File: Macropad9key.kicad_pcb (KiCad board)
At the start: 4 copper layers, 57.9 x 65.7 mm, 83 parts, among them J1 3220-10-0100-00, J2 4POS_2MM, J3 USB4085-GF-A, SW1 CherryMX_WithPCBPins, SW2 CherryMX_WithPCBPins, SW3 CherryMX_WithPCBPins, SW4 CherryMX_WithPCBPins, SW5 CherryMX_WithPCBPins, SW6 CherryMX_WithPCBPins, SW7 CherryMX_WithPCBPins, SW8 CherryMX_WithPCBPins, SW9 CherryMX_WithPCBPins, U1 ATSAMD11D14A-MUT, U2 MCP1700T-3302E-TT, U3 PCA9632DP2

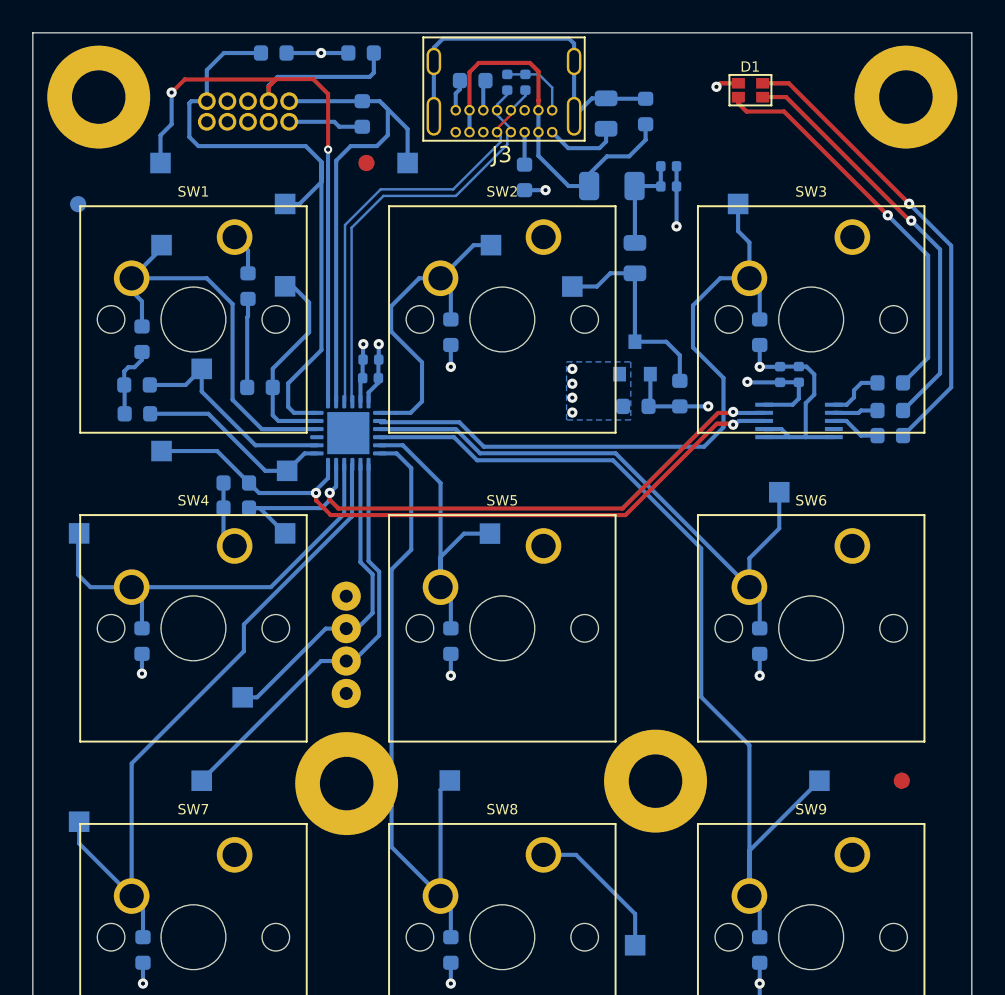
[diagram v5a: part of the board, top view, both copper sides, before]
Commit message: Fix mounting screw hole under ICD header
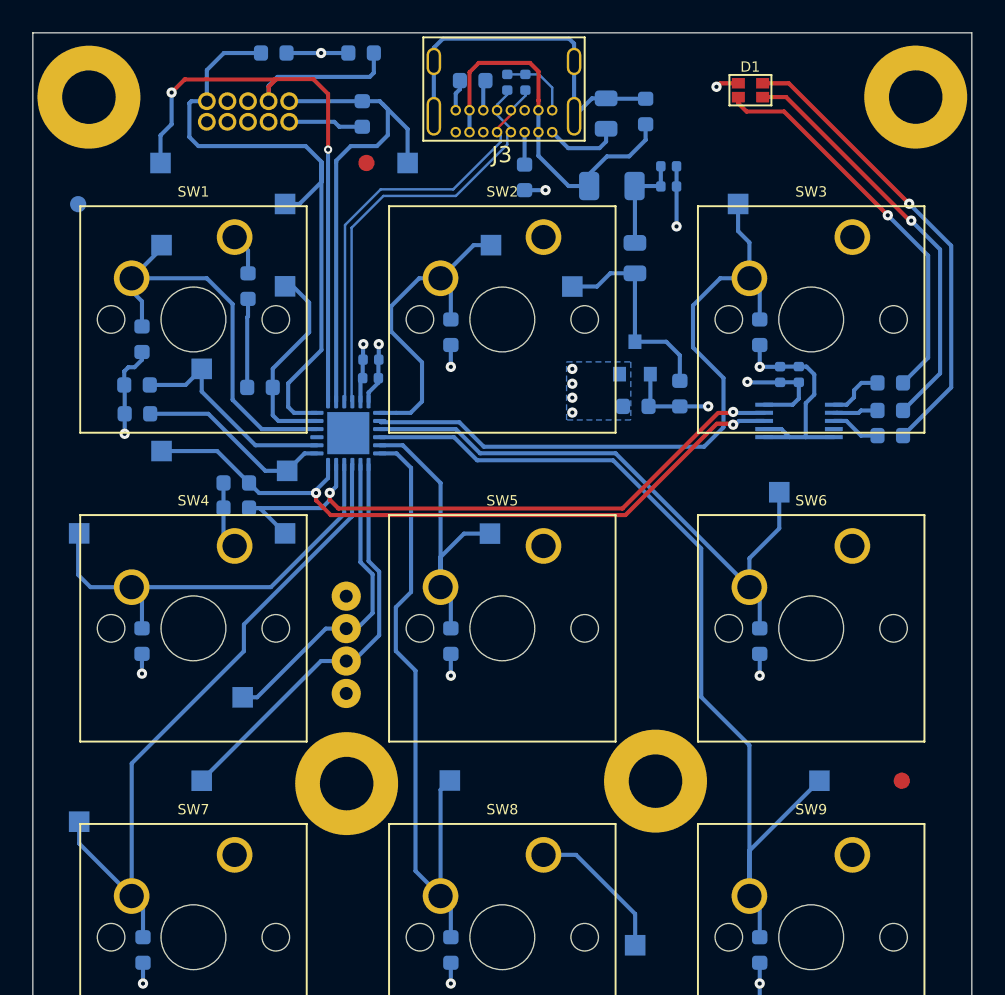
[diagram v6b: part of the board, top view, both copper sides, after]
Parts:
- moved REF** 0.60 mm to (150.5, 82.3)
- moved REF** 0.60 mm to (201.5, 82.3)
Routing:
- net GND: track 57.7 -> 58.9 mm, vias 12 -> 13

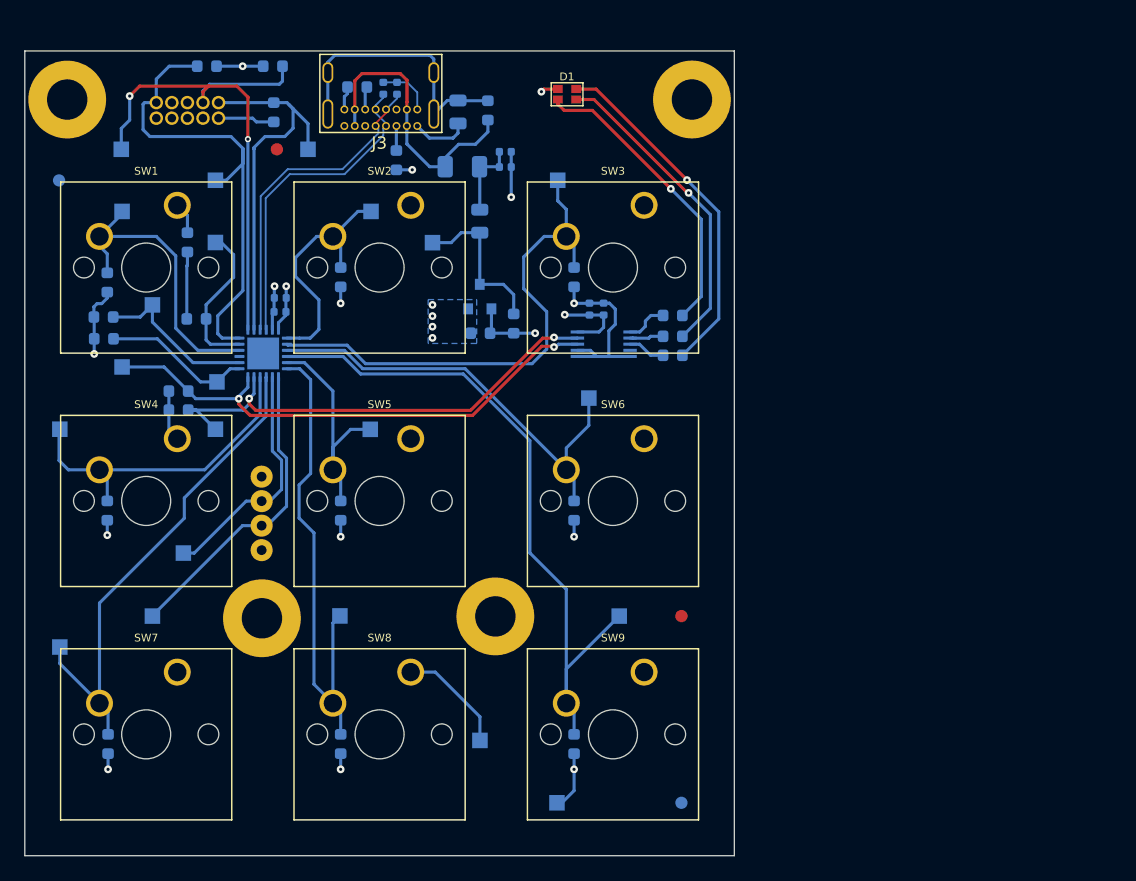
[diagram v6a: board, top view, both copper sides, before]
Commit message: Update titleblock, add fab notes, add drill table
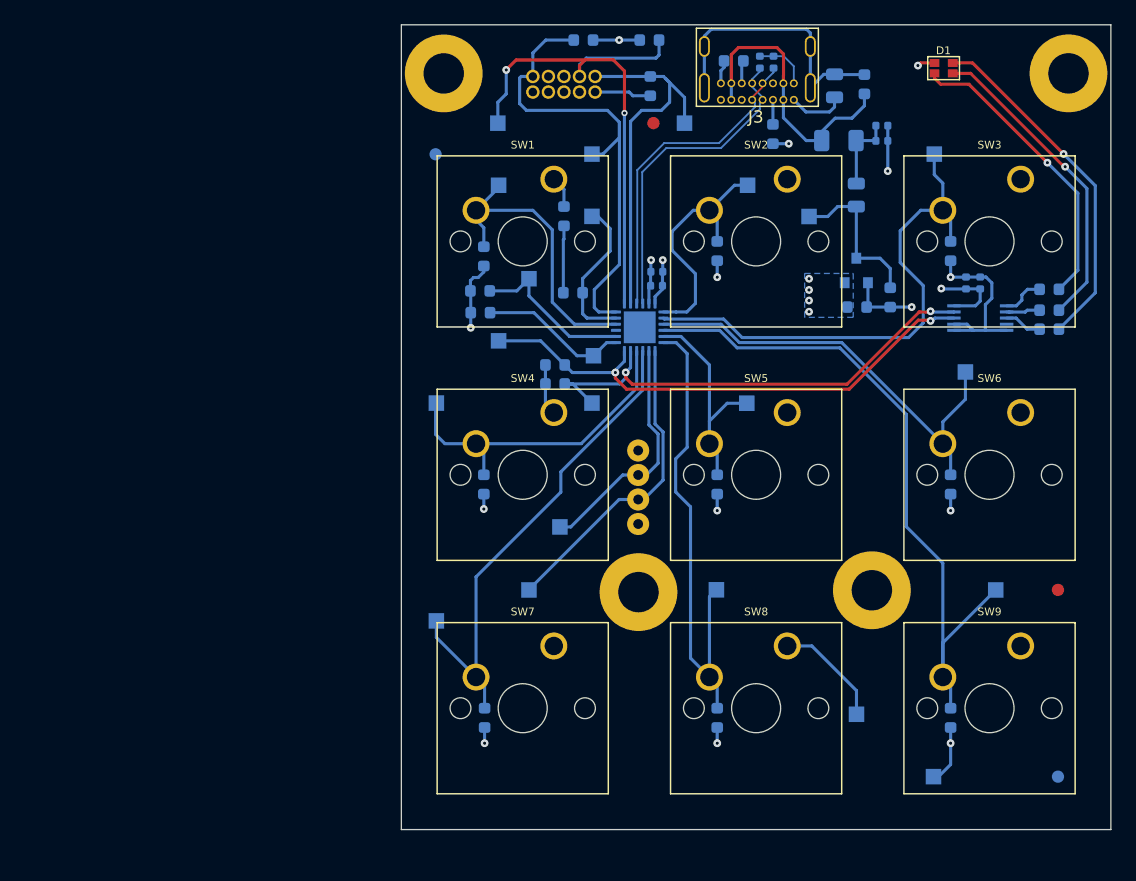
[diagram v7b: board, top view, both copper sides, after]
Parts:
- moved C2 30.8 mm to (198.7, 96.4)
- moved C4 30.8 mm to (215.0, 99.2)
- moved C5 30.8 mm to (225.0, 97.3)
- moved D3 30.8 mm to (208.2, 79.2)
- moved D4 30.8 mm to (207.1, 79.2)
- moved D5 30.8 mm to (215.6, 81.1)
- moved F1 30.8 mm to (213.5, 85.6)
- moved FB1 30.8 mm to (214.9, 90.1)
- moved FB2 30.8 mm to (213.2, 81.2)
- moved J1 30.8 mm to (194.2, 82.3)
- moved J2 30.8 mm to (197.1, 113.9)
- moved R1 30.8 mm to (198.1, 81.2)
- moved R10 30.8 mm to (184.5, 95.1)
- moved R11 30.8 mm to (222.6, 113.7)
- moved R13 30.8 mm to (184.5, 113.7)
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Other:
- board text added: "0.25mm / 0.010" (30 holes) 0.40mm / 0.016" (16 holes) 0.60mm / 0.024" (0 holes + 4 slots) 0.70mm / 0.028" (10 holes) 0.80mm / 0.031" (4 holes) 1.50mm / 0.059" (18 holes) 3.30mm / 0.130" (4 holes) 1.70mm / 0.067" (18 holes) (not plated) 4.00mm / 0.157" (9 holes) (not plated)"
- board text added: "1) BOARD MATERIAL: FR4, 0.062 THICK, 1 Oz Copper 2) SOLDERMASK COLOR: BLACK 3) SILKSCREEN COLOR: WHITE 4) LAYER STACKUP: 1. TOP LAYER 2. VCC 3. GND 4. BOTTOM LAYER 5) DIMENSIONS ARE FOR REFERENCE 6) CONTROLLED IMPEDANCE 1. USB_DP and USB_DN Differential Impedance of 90 Ohms ±15%"
- board text added: "1) PCB SHOULD BE INSPECTED TO IPC-A-610 CLASS II STANDARDS"
- board text added: "Assembled Board Notes:"
- board text added: "Drill Table:"
- board text added: "Raw Board Notes:"
